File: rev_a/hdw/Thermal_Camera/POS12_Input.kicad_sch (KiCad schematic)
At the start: 18 parts

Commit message: added some power supplies
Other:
- note added: "Switch to +3.0V logic?"
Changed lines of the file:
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@@
     (stroke (width 0) (type default))
+  )
+  (text "Switch to +3.0V logic?" (at 104.775 29.21 0)
+    (effects (font (size 5.08 5.08) (thickness 1.016) bold (color 194 0 0 1)) (justify left bottom))
   )
   (text "UVLO threshold set to 10.8V\nOVLO threshold set to 13.2V\n\nMODE set to Circuit Breaker with Auto-Retry\n\nOutput Current Limit set to 1.2A"

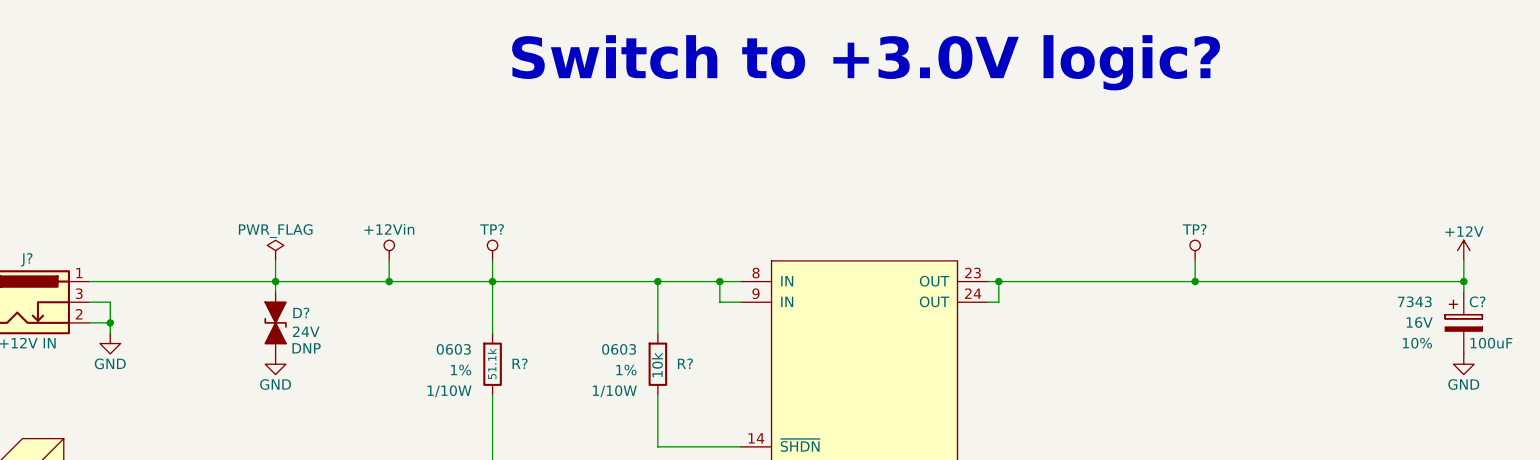
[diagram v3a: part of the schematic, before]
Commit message: added new telemetry circuits
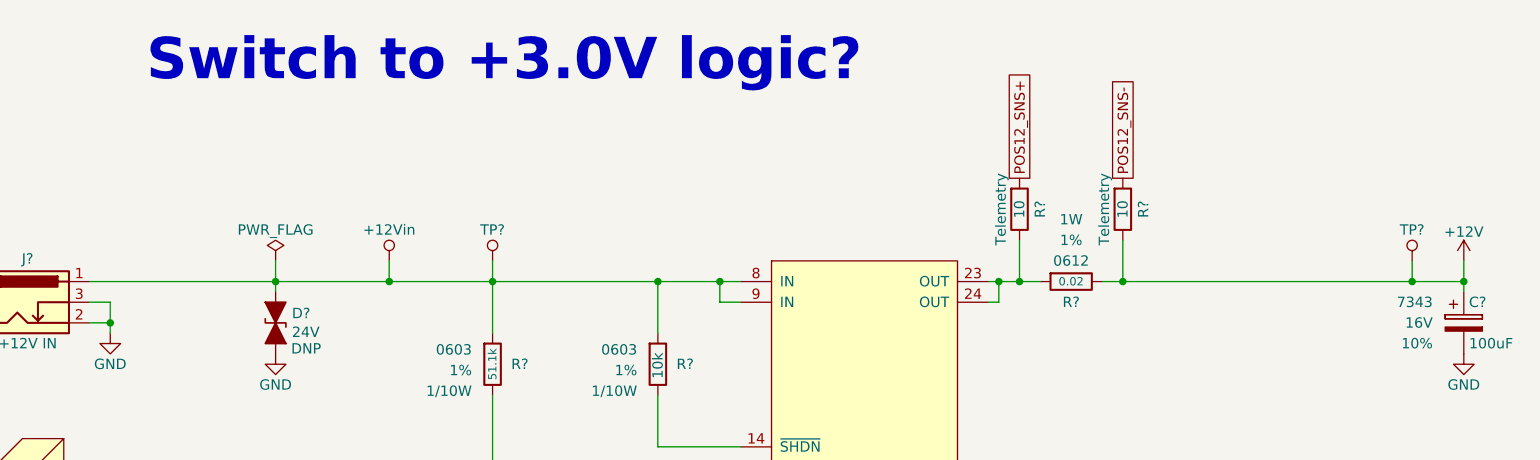
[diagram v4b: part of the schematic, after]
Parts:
- added R? (x2): 10, Resistors_SMD:R_0603, symbol Custom_Library:R_Custom
- added R?: 0.02, Resistors_SMD:R_0612, symbol Custom_Library:R_Custom
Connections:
- net +12V: now also R?.2, R?.2; no longer U?.23 (OUT), U?.24 (OUT)
- new net: R?.1, R?.2, U?.23 (OUT), U?.24 (OUT)
- new net POS12_SNS+: R?.1
- new net POS12_SNS-: R?.1
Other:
- moved on the sheet: TP?

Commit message: duplicated telemetry for all rails, added random tweaks to logic levels of signals
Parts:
- removed R?: 5.11k, Resistors_SMD:R_0603, symbol Custom_Library:R_Custom
- added R?: 1.15k, Resistors_SMD:R_0603, symbol Custom_Library:R_Custom
- R?: value 13k -> 5.11k
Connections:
- net GND: now also R?.2
- net POS12_PGOOD: now also R?.1
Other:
- note added: "+3.0V logic level at +13.2Vin"
- note removed: "+3.3V Logic Level"
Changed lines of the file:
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@@
     (effects (font (size 1.27 1.27)) (justify left bottom))
   )
-  (text "+3.3V Logic Level" (at 188.214 94.488 0)
+  (text "+3.0V logic level at +13.2Vin" (at 188.214 94.488 0)
     (effects (font (size 1.27 1.27)) (justify left bottom))
   )
@@
     )
   )
+  (symbol (lib_id "Custom_Library:R_Custom") (at 173.99 106.68 0) (unit 1)
+    (in_bom yes) (on_board yes) (dnp no)
+    (property "Reference" "R?" (at 171.704 106.68 0)
+      (effects (font (size 1.27 1.27)) (justify right))
+    )
+    (property "Value" "1.15k" (at 173.99 106.68 90)
+      (effects (font (size 1.016 1.016)))
+    )
+    (property "Footprint" "Resistors_SMD:R_0603" (at 173.99 106.68 0)
+      (effects (font (size 1.27 1.27)) hide)
+    )
+    (property "Datasheet" "" (at 173.99 106.68 0)
+      (effects (font (size 1.27 1.27)) hide)
+    )
+    (property "display_footprint" "0603" (at 176.53 104.902 0)
+      (effects (font (size 1.27 1.27)) (justify left))
+    )
+    (property "Tolerance" "1%" (at 176.53 107.442 0)
+      (effects (font (size 1.27 1.27)) (justify left))
+    )
+    (property "Wattage" "1/10W" (at 176.53 109.982 0)
+      (effects (font (size 1.27 1.27)) (justify left))
+    )
+    (property "Digi-Key PN" "541-1.15KHCT-ND" (at 181.61 96.52 0)
+      (effects (font (size 1.524 1.524)) hide)
+    )
+    (pin "1")
+    (pin "2")
+    (instances
+      (project "Thermal_Camera"
+        (path "/4bd21e0b-5408-4b93-866e-c82ac5b31fa9/83e737bd-36e4-4450-be79-c684a42552df"
+          (reference "R?") (unit 1)
+        )
+      )
+      (project "Analog_Clock"
+        (path "/4c0a1b3a-0b35-42a0-8d96-e340db30946e/00000000-0000-0000-0000-00005d6c0d23"
+          (reference "R?") (unit 1)
+        )
+        (path "/4c0a1b3a-0b35-42a0-8d96-e340db30946e/00000000-0000-0000-0000-00005e939cff"
+          (reference "R?") (unit 1)
+        )
+        (path "/4c0a1b3a-0b35-42a0-8d96-e340db30946e/00000000-0000-0000-0000-00005d77a516"
+          (reference "R?") (unit 1)
+        )
+        (path "/4c0a1b3a-0b35-42a0-8d96-e340db30946e/00000000-0000-0000-0000-00005d6b2673"
+          (reference "R?") (unit 1)
+        )
+      )
+      (project "USB_Hub"
+        (path "/e85aac8c-404c-45dd-bda3-1057cae83baf/00000000-0000-0000-0000-00005f41a7ad"
+          (reference "R202") (unit 1)
+        )
+      )
+    )
+  )
   (symbol (lib_id "Custom_Library:R_Custom") (at 193.04 128.27 0) (unit 1)
     (in_bom yes) (on_board yes) (dnp no)
@@
     )
   )
-  (symbol (lib_id "Custom_Library:R_Custom") (at 173.99 106.68 0) (unit 1)
-    (in_bom yes) (on_board yes) (dnp no)
-    (property "Reference" "R?" (at 171.704 106.68 0)
-      (effects (font (size 1.27 1.27)) (justify right))
-    )
-    (property "Value" "5.11k" (at 173.99 106.68 90)
-      (effects (font (size 1.016 1.016)))
-    )
-    (property "Footprint" "Resistors_SMD:R_0603" (at 173.99 106.68 0)
-      (effects (font (size 1.27 1.27)) hide)
-    )
-    (property "Datasheet" "" (at 173.99 106.68 0)
-      (effects (font (size 1.27 1.27)) hide)
-    )
-    (property "display_footprint" "0603" (at 176.53 104.902 0)
-      (effects (font (size 1.27 1.27)) (justify left))
-    )
-    (property "Tolerance" "1%" (at 176.53 107.442 0)
-      (effects (font (size 1.27 1.27)) (justify left))
-    )
-    (property "Wattage" "1/10W" (at 176.53 109.982 0)
-      (effects (font (size 1.27 1.27)) (justify left))
-    )
-    (property "Digi-Key PN" "541-5.11KHCT-ND" (at 181.61 96.52 0)
-      (effects (font (size 1.524 1.524)) hide)
-    )
-    (pin "1")
-    (pin "2")
-    (instances
-      (project "Thermal_Camera"
-        (path "/4bd21e0b-5408-4b93-866e-c82ac5b31fa9/83e737bd-36e4-4450-be79-c684a42552df"
-          (reference "R?") (unit 1)
-        )
-      )
-      (project "Analog_Clock"
-        (path "/4c0a1b3a-0b35-42a0-8d96-e340db30946e/00000000-0000-0000-0000-00005d6c0d23"
-          (reference "R?") (unit 1)
-        )
-        (path "/4c0a1b3a-0b35-42a0-8d96-e340db30946e/00000000-0000-0000-0000-00005e939cff"
-          (reference "R?") (unit 1)
-        )
-        (path "/4c0a1b3a-0b35-42a0-8d96-e340db30946e/00000000-0000-0000-0000-00005d77a516"
-          (reference "R?") (unit 1)
-        )
-        (path "/4c0a1b3a-0b35-42a0-8d96-e340db30946e/00000000-0000-0000-0000-00005d6b2673"
-          (reference "R?") (unit 1)
-        )
-      )
-      (project "USB_Hub"
-        (path "/e85aac8c-404c-45dd-bda3-1057cae83baf/00000000-0000-0000-0000-00005f41a7ad"
-          (reference "R207") (unit 1)
-        )
-      )
-    )
-  )
   (symbol (lib_id "Custom_Library:R_Custom") (at 172.72 128.27 0) (unit 1)
     (in_bom yes) (on_board yes) (dnp no)
@@
       (effects (font (size 1.27 1.27)) (justify right))
     )
-    (property "Value" "13k" (at 173.99 95.25 90)
-      (effects (font (size 1.27 1.27)))
+    (property "Value" "5.11k" (at 173.99 95.25 90)
+      (effects (font (size 1.016 1.016)))
     )
     (property "Footprint" "Resistors_SMD:R_0603" (at 173.99 95.25 0)

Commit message: added PIC32 bypass, SD card load switch, other random junk
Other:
- note removed: "Switch to +3.0V logic?"
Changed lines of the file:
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@@
     (stroke (width 0) (type default))
-  )
-  (text "Switch to +3.0V logic?" (at 60.325 29.21 0)
-    (effects (font (size 5.08 5.08) (thickness 1.016) bold (color 194 0 0 1)) (justify left bottom))
   )
   (text "UVLO threshold set to 10.8V\nOVLO threshold set to 13.2V\n\nMODE set to Circuit Breaker with Auto-Retry\n\nOutput Current Limit set to 1.2A"
